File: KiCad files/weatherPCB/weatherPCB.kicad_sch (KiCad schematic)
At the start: 33 parts, among them J1 Expansion header, J3 USB_C_Receptacle_USB2.0_16P, SW1 RESET, SW2 BOOT, U1 OPT3001DNPR, U16 ESP32-S3-WROOM-1, U17 USBLC6-2SC6, U18 BME280, U19 LM1117DT-ADJ

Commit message: Improved usb routing on pcb
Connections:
- net EN: now also C1.2; no longer C1.1
- net GND: now also C1.1; no longer C1.2
- no-connect marks 30 -> 32
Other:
- moved on the sheet: C1

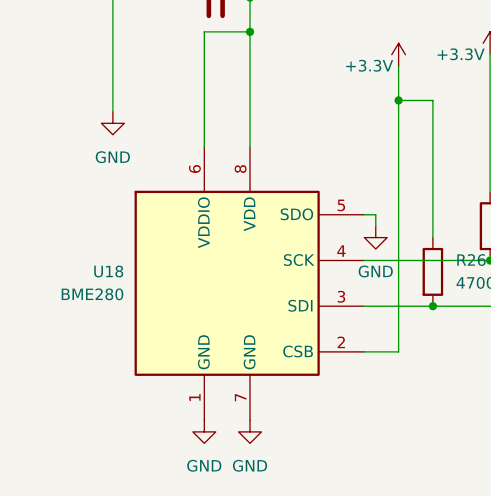
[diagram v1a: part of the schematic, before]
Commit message: replaced bme280 with bme680
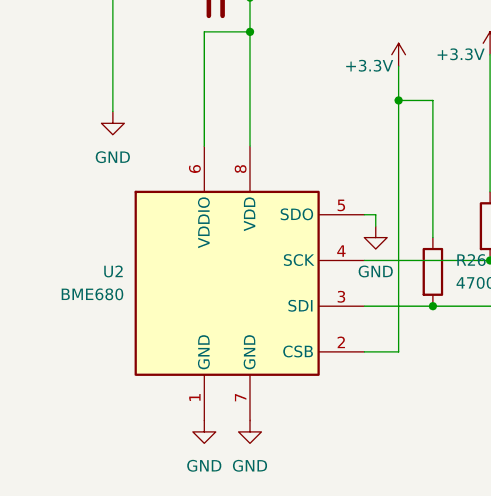
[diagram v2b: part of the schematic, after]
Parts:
- removed U18: BME280, Package_LGA:Bosch_LGA-8_2.5x2.5mm_P0.65mm_ClockwisePinNumbering, symbol Sensor:BME280
- added U2: BME680, Package_LGA:Bosch_LGA-8_3x3mm_P0.8mm_ClockwisePinNumbering, symbol Sensor:BME680
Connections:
- net +3.3V: now also U2.2 (CSB), U2.6 (VDDIO), U2.8 (VDD)
- net GND: now also U2.1 (GND), U2.5 (SDO), U2.7 (GND)
- net SCL: now also U2.4 (SCK)
- net SDA: now also U2.3 (SDI)
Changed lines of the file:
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@@
+	)
+	(symbol
+		(lib_id "Sensor:BME680")
+		(at 57.15 166.37 0)
+		(unit 1)
+		(exclude_from_sim no)
+		(in_bom yes)
+		(on_board yes)
+		(dnp no)
+		(fields_autoplaced yes)
+		(property "Reference" "U2"
+			(at 45.72 165.0999 0)
+			(effects
+				(font
+					(size 1.27 1.27)
+				)
+				(justify right)
+			)
+		)
+		(property "Value" "BME680"
+			(at 45.72 167.6399 0)
+			(effects
+				(font
+					(size 1.27 1.27)
+				)
+				(justify right)
+			)
+		)
+		(property "Footprint" "Package_LGA:Bosch_LGA-8_3x3mm_P0.8mm_ClockwisePinNumbering"
+			(at 93.98 177.8 0)
+			(effects
+				(font
+					(size 1.27 1.27)
+				)
+				(hide yes)
+			)
+		)
+		(property "Datasheet" "https://ae-bst.resource.bosch.com/media/_tech/media/datasheets/BST-BME680-DS001.pdf"
+			(at 57.15 171.45 0)
+			(effects
+				(font
+					(size 1.27 1.27)
+				)
+				(hide yes)
+			)
+		)
+		(property "Description" "4-in-1 sensor, gas, humidity, pressure, temperature, I2C and SPI interface, 1.71-3.6V, LGA-8"
+			(at 57.15 166.37 0)
+			(effects
+				(font
+					(size 1.27 1.27)
+				)
+				(hide yes)
+			)
+		)
+		(pin "6"
+		)
+		(pin "1"
+		)
+		(pin "8"
+		)
+		(pin "2"
+		)
+		(pin "5"
+		)
+		(pin "3"
+		)
+		(pin "7"
+		)
+		(pin "4"
+		)
+		(instances
+			(project ""
+				(path "/d2821ffd-b5a0-410f-bd0d-f94a66a717da"
+					(reference "U2")
+					(unit 1)
+				)
+			)
+		)
 	)
 	(symbol
@@
 					(unit 1)
 				)
-			)
-		)
-	)
-	(symbol
-		(lib_id "Sensor:BME280")
-		(at 57.15 166.37 0)
-		(unit 1)
-		(exclude_from_sim no)
-		(in_bom yes)
-		(on_board yes)
-		(dnp no)
-		(fields_autoplaced yes)
-		(property "Reference" "U18"
-			(at 45.72 165.0999 0)
-			(effects
-				(font
-					(size 1.27 1.27)
-				)
-				(justify right)
-			)
-		)
-		(property "Value" "BME280"
-			(at 45.72 167.6399 0)
-			(effects
-				(font
-					(size 1.27 1.27)
-				)
-				(justify right)
-			)
-		)
-		(property "Footprint" "Package_LGA:Bosch_LGA-8_2.5x2.5mm_P0.65mm_ClockwisePinNumbering"
-			(at 95.25 177.8 0)
-			(effects
-				(font
-					(size 1.27 1.27)
-				)
-				(hide yes)
-			)
-		)
-		(property "Datasheet" "https://www.bosch-sensortec.com/media/boschsensortec/downloads/datasheets/bst-bme280-ds002.pdf"
-			(at 57.15 171.45 0)
-			(effects
-				(font
-					(size 1.27 1.27)
-				)
-				(hide yes)
-			)
-		)
-		(property "Description" "3-in-1 sensor, humidity, pressure, temperature, I2C and SPI interface, 1.71-3.6V, LGA-8"
-			(at 57.15 166.37 0)
-			(effects
-				(font
-					(size 1.27 1.27)
-				)
-				(hide yes)
-			)
-		)
-		(pin "7"
-		)
-		(pin "5"
-		)
-		(pin "4"
-		)
-		(pin "2"
-		)
-		(pin "6"
-		)
-		(pin "8"
-		)
-		(pin "1"
-		)
-		(pin "3"
-		)
-		(instances
-			(project "weatherPCB"
-				(path "/d2821ffd-b5a0-410f-bd0d-f94a66a717da"
-					(reference "U18")
-					(unit 1)
-				)
